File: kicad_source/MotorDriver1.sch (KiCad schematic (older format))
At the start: 17 parts, among them P5 CONN_01X04, P6 CONN_01X05, U2 TMC5130A-TA

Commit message: generated pdf files
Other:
- note added: "Copyright generationmake 2019\nsee full project documentation at https://github.com/generationmake/StepperMotorFeatherWing"
- note removed: "Copyright generationmake 2019\nsee full project documentation at http://arduhmi.generationmake.de"
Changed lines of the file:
@@
 Sheet 6 6
 Title "HighPowerMotorFeatherWing"
-Date "2019-12-01"
+Date "2019-12-31"
 Rev "1.0"
 Comp "generationmake"
@@
 $EndDescr
 Text Notes 500  650  0    47   ~ 0
-Copyright generationmake 2019\nsee full project documentation at http://arduhmi.generationmake.de
+Copyright generationmake 2019\nsee full project documentation at https://github.com/generationmake/StepperMotorFeatherWing
 Text Notes 7000 6900 0    43   ~ 0
 You may redistribute and modify this documentation under the terms of the CERN OHL v.1.2. (http://ohwr.org/cernohl). \nThis documentation is distributed WITHOUT ANY EXPRESS OR IMPLIED WARRANTY, INCLUDING OF MERCHANTABILITY, SATISFACTORY \nQUALITY AND FITNESS FOR A PARTICULAR PURPOSE. Please see the CERN OHL v.1.2  for applicable conditions

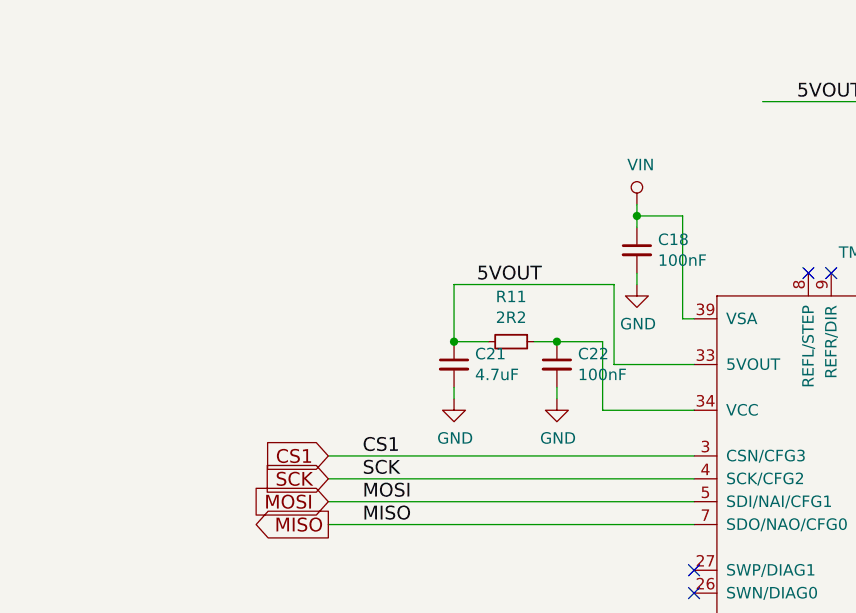
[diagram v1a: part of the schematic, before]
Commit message: added external supply for +5V for TMC5130
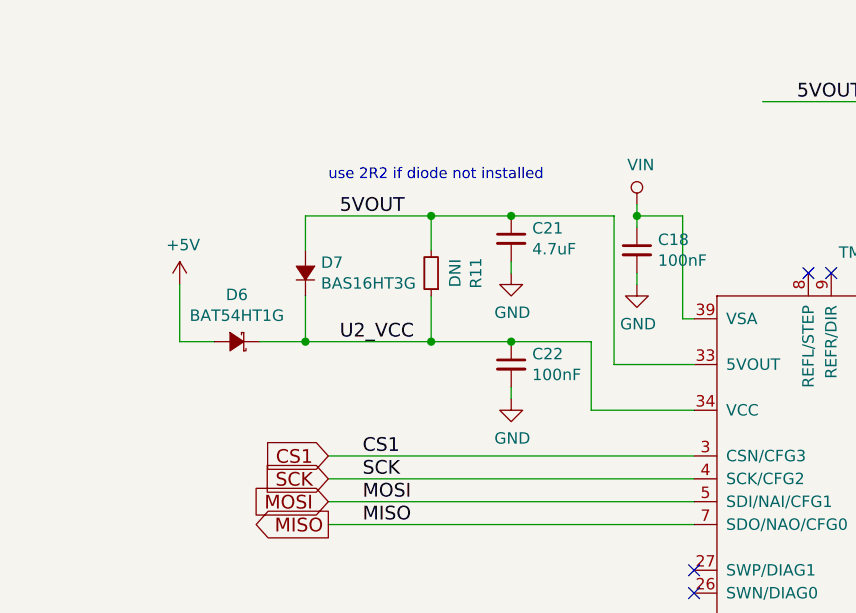
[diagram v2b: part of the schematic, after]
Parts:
- added D6: BAT54HT1G, diodes:SOD-323, symbol devices:D_Schottky_Small
- added D7: BAS16HT3G, diodes:SOD-323, symbol devices:D_Small
- R11: value 2R2 -> DNI
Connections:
- net 5VOUT: now also D7.2 (A)
- net U2_VCC: now reaches C22.1, R11.1, U2.34 (VCC)
- net U2_VCC: now also D6.1 (K), D7.1 (K)
- new net +5V: D6.2 (A)
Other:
- note added: "use 2R2 if diode not installed"
- moved on the sheet: C21, C22, R11
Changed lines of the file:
@@
 L devices:C_0603 C22
 U 1 1 5DF40D32
-P 4450 2450
-F 0 "C22" H 4542 2496 50  0000 L CNN
-F 1 "100nF" H 4542 2405 50  0000 L CNN
-F 2 "capacitors:C_0603" H 4450 2300 50  0001 C CNN
-F 3 "" H 4450 2450 50  0000 C CNN
-	1    4450 2450
+P 4250 2450
+F 0 "C22" H 4342 2496 50  0000 L CNN
+F 1 "100nF" H 4342 2405 50  0000 L CNN
+F 2 "capacitors:C_0603" H 4250 2300 50  0001 C CNN
+F 3 "" H 4250 2450 50  0000 C CNN
+	1    4250 2450
 	1    0    0    -1
 $EndComp
@@
 L devices:C_0603 C21
 U 1 1 5DED18DA
-P 4000 2450
-F 0 "C21" H 4092 2496 50  0000 L CNN
-F 1 "4.7uF" H 4092 2405 50  0000 L CNN
-F 2 "capacitors:C_0603" H 4000 2300 50  0001 C CNN
-F 3 "" H 4000 2450 50  0000 C CNN
-	1    4000 2450
+P 4250 1900
+F 0 "C21" H 4342 1946 50  0000 L CNN
+F 1 "4.7uF" H 4342 1855 50  0000 L CNN
+F 2 "capacitors:C_0603" H 4250 1750 50  0001 C CNN
+F 3 "" H 4250 1900 50  0000 C CNN
+	1    4250 1900
 	1    0    0    -1
 $EndComp
@@
 L devices:R_0603 R11
 U 1 1 5DED18DC
-P 4250 2350
-F 0 "R11" V 4054 2350 50  0000 C CNN
-F 1 "2R2" V 4145 2350 50  0000 C CNN
-F 2 "resistors:R_0603" H 4250 2200 50  0001 C CNN
-F 3 "" H 4250 2350 50  0000 C CNN
-	1    4250 2350
-	0    1    1    0
+P 3900 2050
+F 0 "R11" V 3704 2050 50  0000 C CNN
+F 1 "DNI" V 3795 2050 50  0000 C CNN
+F 2 "resistors:R_0603" H 3900 1900 50  0001 C CNN
+F 3 "" H 3900 2050 50  0000 C CNN
+	1    3900 2050
+	-1   0    0    1
 $EndComp
 $Comp
 L power-supply:GND #PWR048
 U 1 1 5DED18DD
-P 4450 2600
-F 0 "#PWR048" H 4450 2350 50  0001 C CNN
-F 1 "GND" H 4455 2427 50  0000 C CNN
-F 2 "" H 4450 2600 50  0000 C CNN
-F 3 "" H 4450 2600 50  0000 C CNN
-	1    4450 2600
+P 4250 2600
+F 0 "#PWR048" H 4250 2350 50  0001 C CNN
+F 1 "GND" H 4255 2427 50  0000 C CNN
+F 2 "" H 4250 2600 50  0000 C CNN
+F 3 "" H 4250 2600 50  0000 C CNN
+	1    4250 2600
 	1    0    0    -1
 $EndComp
@@
 L power-supply:GND #PWR047
 U 1 1 5DED18DE
-P 4000 2600
-F 0 "#PWR047" H 4000 2350 50  0001 C CNN
-F 1 "GND" H 4005 2427 50  0000 C CNN
-F 2 "" H 4000 2600 50  0000 C CNN
-F 3 "" H 4000 2600 50  0000 C CNN
-	1    4000 2600
+P 4250 2050
+F 0 "#PWR047" H 4250 1800 50  0001 C CNN
+F 1 "GND" H 4255 1877 50  0000 C CNN
+F 2 "" H 4250 2050 50  0000 C CNN
+F 3 "" H 4250 2050 50  0000 C CNN
+	1    4250 2050
 	1    0    0    -1
 $EndComp
@@
 	4800 1800 4800 1750
 Wire Wire Line
-	5050 2650 4650 2650
-Wire Wire Line
-	4650 2650 4650 2350
-Wire Wire Line
-	4650 2350 4450 2350
-Wire Wire Line
-	4450 2350 4350 2350
-Connection ~ 4450 2350
-Wire Wire Line
 	5050 2450 4700 2450
 Wire Wire Line
-	4700 2450 4700 2100
-Wire Wire Line
-	4700 2100 4000 2100
-Wire Wire Line
-	4000 2100 4000 2350
-Wire Wire Line
-	4000 2350 4150 2350
-Connection ~ 4000 2350
-Wire Wire Line
-	4000 2550 4000 2600
-Wire Wire Line
-	4450 2550 4450 2600
+	4250 2000 4250 2050
+Wire Wire Line
+	4250 2550 4250 2600
 Wire Wire Line
 	5050 3850 4950 3850
@@
 Text Label 6350 6000 0    60   ~ 0
 ENCN
-Text Label 4100 2100 0    60   ~ 0
+Text Label 3500 1800 0    60   ~ 0
 5VOUT
 $Comp
@@
 Text Label 7700 3250 0    60   ~ 0
 OB2
+Wire Wire Line
+	4600 2650 4600 2350
+Wire Wire Line
+	4600 2350 4250 2350
+Wire Wire Line
+	4600 2650 5050 2650
+Wire Wire Line
+	4700 1800 4250 1800
+Wire Wire Line
+	4700 1800 4700 2450
+Text Notes 3450 1650 0    47   ~ 0
+use 2R2 if diode not installed
+$Comp
+L devices:D_Small D7
+U 1 1 5F04EB24
+P 3350 2050
+F 0 "D7" V 3396 1982 50  0000 R CNN
+F 1 "BAS16HT3G" V 3305 1982 50  0000 R CNN
+F 2 "diodes:SOD-323" V 3350 2050 50  0001 C CNN
+F 3 "" V 3350 2050 50  0000 C CNN
+	1    3350 2050
+	0    -1   -1   0
+$EndComp
+$Comp
+L devices:D_Schottky_Small D6
+U 1 1 5F04F43A
+P 3050 2350
+F 0 "D6" H 3050 2145 50  0000 C CNN
+F 1 "BAT54HT1G" H 3050 2236 50  0000 C CNN
+F 2 "diodes:SOD-323" V 3050 2350 50  0001 C CNN
+F 3 "" V 3050 2350 50  0000 C CNN
+	1    3050 2350
+	-1   0    0    1
+$EndComp
+$Comp
+L power-supply:+5V #PWR094
+U 1 1 5F0508C0
+P 2800 2100
+F 0 "#PWR094" H 2800 1950 50  0001 C CNN
+F 1 "+5V" H 2815 2273 50  0000 C CNN
+F 2 "" H 2800 2100 50  0000 C CNN
+F 3 "" H 2800 2100 50  0000 C CNN
+	1    2800 2100
+	1    0    0    -1
+$EndComp
+Wire Wire Line
+	3150 2350 3350 2350
+Connection ~ 4250 2350
+Wire Wire Line
+	4250 1800 3900 1800
+Wire Wire Line
+	3350 1800 3350 1950
+Connection ~ 4250 1800
+Wire Wire Line
+	3350 2150 3350 2350
+Connection ~ 3350 2350
+Wire Wire Line
+	3350 2350 3900 2350
+Wire Wire Line
+	3900 2150 3900 2350
+Connection ~ 3900 2350
+Wire Wire Line
+	3900 2350 4250 2350
+Wire Wire Line
+	3900 1950 3900 1800
+Connection ~ 3900 1800
+Wire Wire Line
+	3900 1800 3350 1800
+Wire Wire Line
+	2950 2350 2800 2350
+Wire Wire Line
+	2800 2350 2800 2100
+Text Label 3500 2350 0    60   ~ 0
+U2_VCC
 $EndSCHEMATC

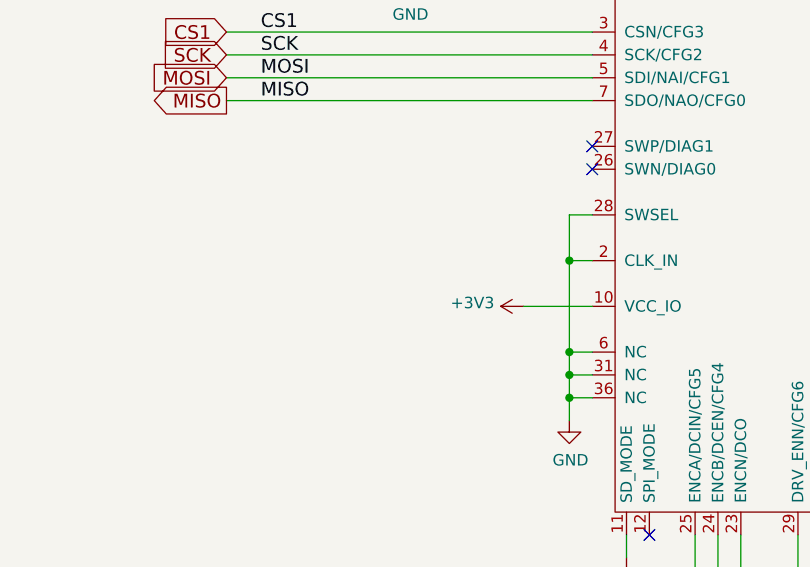
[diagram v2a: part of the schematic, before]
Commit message: added clock generator as common clock for both stepper drivers
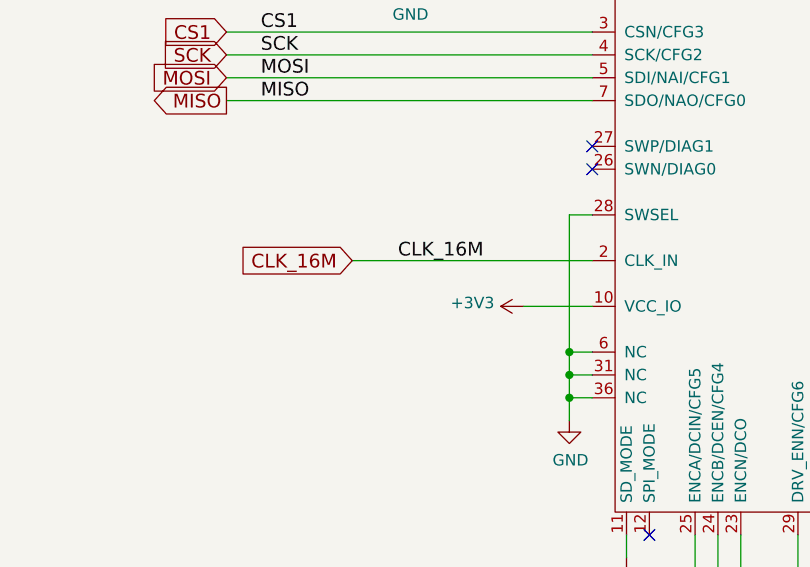
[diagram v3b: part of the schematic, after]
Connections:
- net GND: no longer U2.2 (CLK_IN)
- new net CLK_16M: U2.2 (CLK_IN)
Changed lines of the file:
@@
 $Descr A4 11693 8268
 encoding utf-8
-Sheet 6 6
+Sheet 4 6
 Title "HighPowerMotorFeatherWing"
 Date "2019-12-31"
@@
 Wire Wire Line
 	4250 2550 4250 2600
-Wire Wire Line
-	5050 3850 4950 3850
-Wire Wire Line
-	4950 3850 4950 4250
 Connection ~ 4950 4250
 $Comp
@@
 Wire Wire Line
 	5050 3650 4950 3650
-Wire Wire Line
-	4950 3650 4950 3850
-Connection ~ 4950 3850
 $Comp
 L power-supply:GND #PWR054
@@
 Text Label 3500 2350 0    60   ~ 0
 U2_VCC
+Text GLabel 4000 3850 0    60   Input ~ 0
+CLK_16M
+Wire Wire Line
+	4950 3650 4950 4250
+Wire Wire Line
+	5050 3850 4000 3850
+Text Label 4200 3850 0    60   ~ 0
+CLK_16M
 $EndSCHEMATC
